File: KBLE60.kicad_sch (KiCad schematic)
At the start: 69 parts

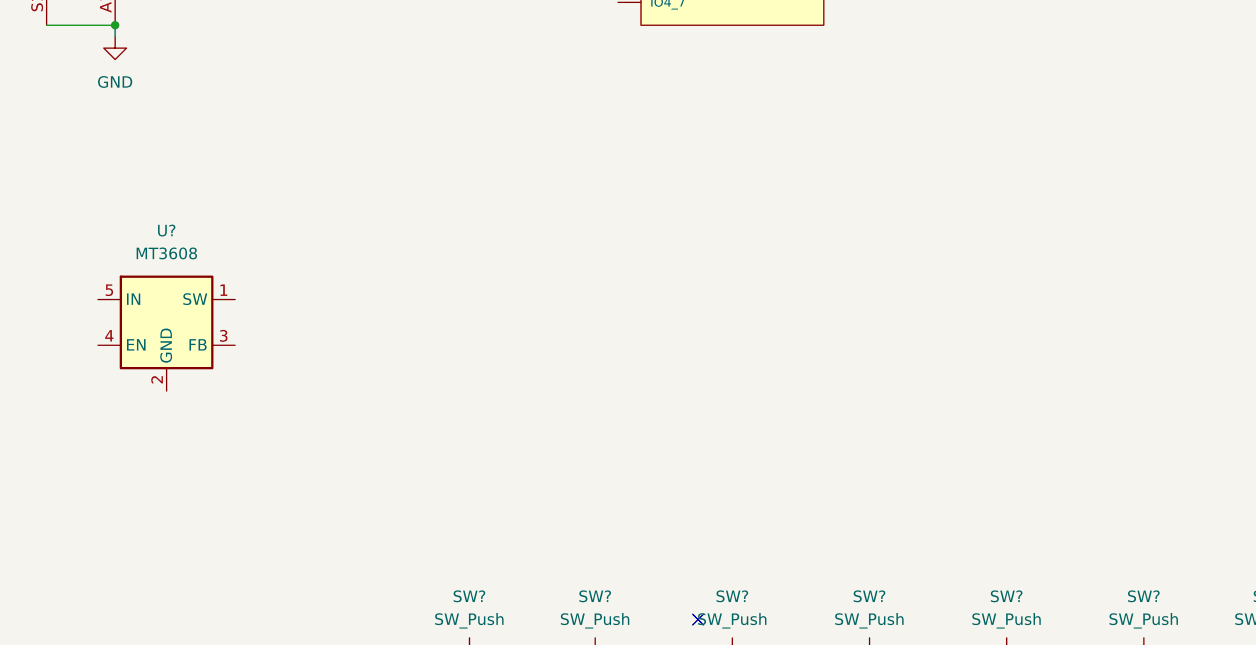
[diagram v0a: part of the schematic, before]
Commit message: battery charging ic
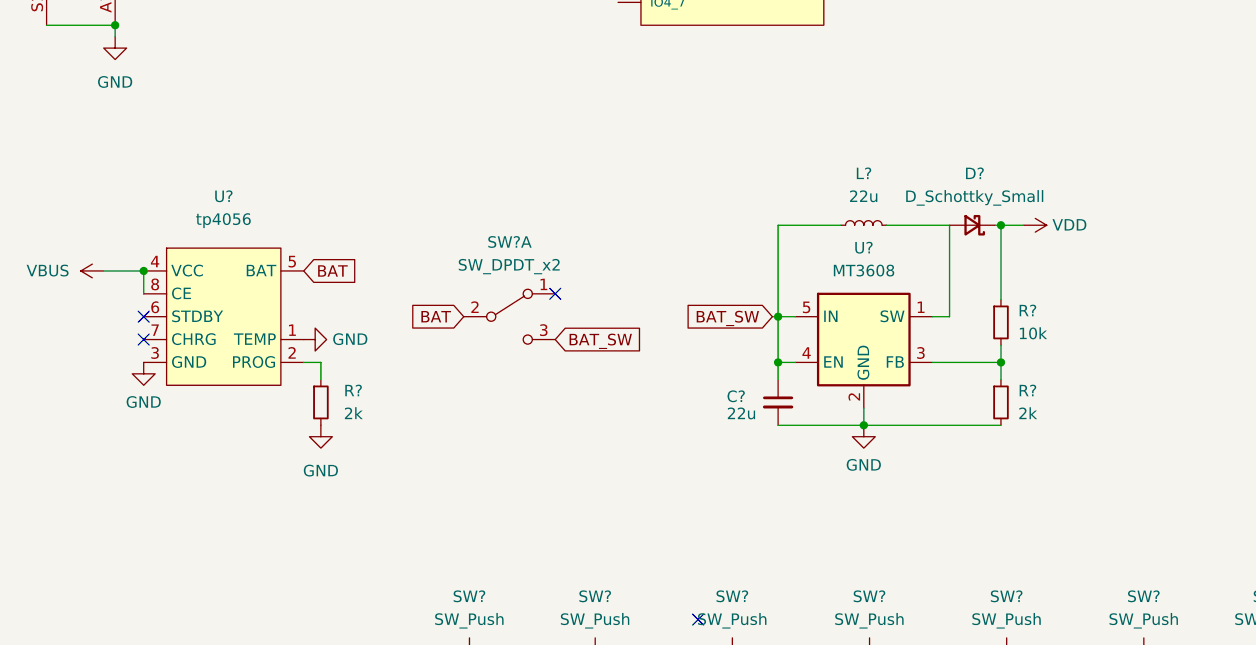
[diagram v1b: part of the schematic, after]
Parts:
- added C?: 22u, symbol Device:C_Small
- added D?: D_Schottky_Small, symbol Device:D_Schottky_Small
- added L?: 22u, symbol Device:L_Small
- added R?: 10k, symbol Device:R_Small
- added R? (x2): 2k, symbol Device:R_Small
- added SW?: SW_DPDT_x2, symbol Switch:SW_DPDT_x2
- added U?: tp4056, Package_SO:TSSOP-8_3x3mm_P0.65mm, symbol TP4056:tp4056
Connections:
- net GND: now also U?.2 (GND), C?.2, R?.2, R?.2, U?.1 (TEMP), U?.3 (GND)
- net VBUS: now also U?.4 (VCC), U?.8 (CE)
- net VDD: now also D?.1 (K), R?.1
- net at U?.1 (SW): now also D?.2 (A), L?.2
- net at U?.3 (FB): now also R?.1, R?.2
- net BAT_SW: now reaches U?.4 (EN)
- net BAT_SW: now also U?.5 (IN), C?.1, L?.1, SW?.3 (C)
- new net: R?.1, U?.2 (PROG)
- new net BAT: SW?.2 (B), U?.5 (BAT)
- no-connect marks 12 -> 15
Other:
- moved on the sheet: U?

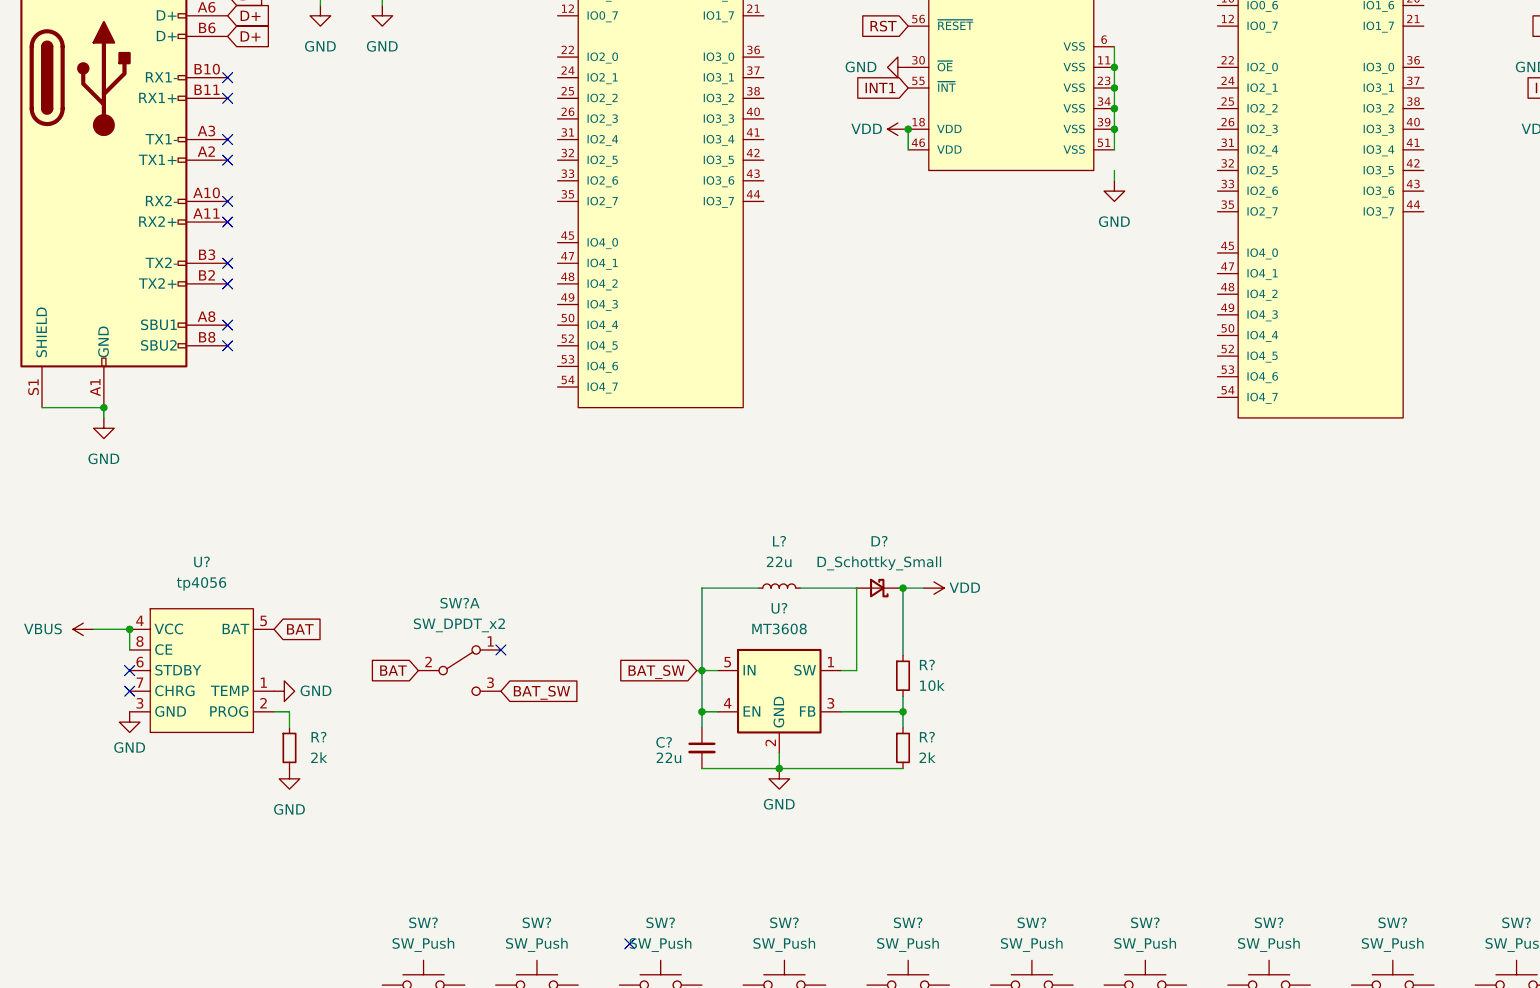
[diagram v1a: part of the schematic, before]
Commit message: Add protection ic
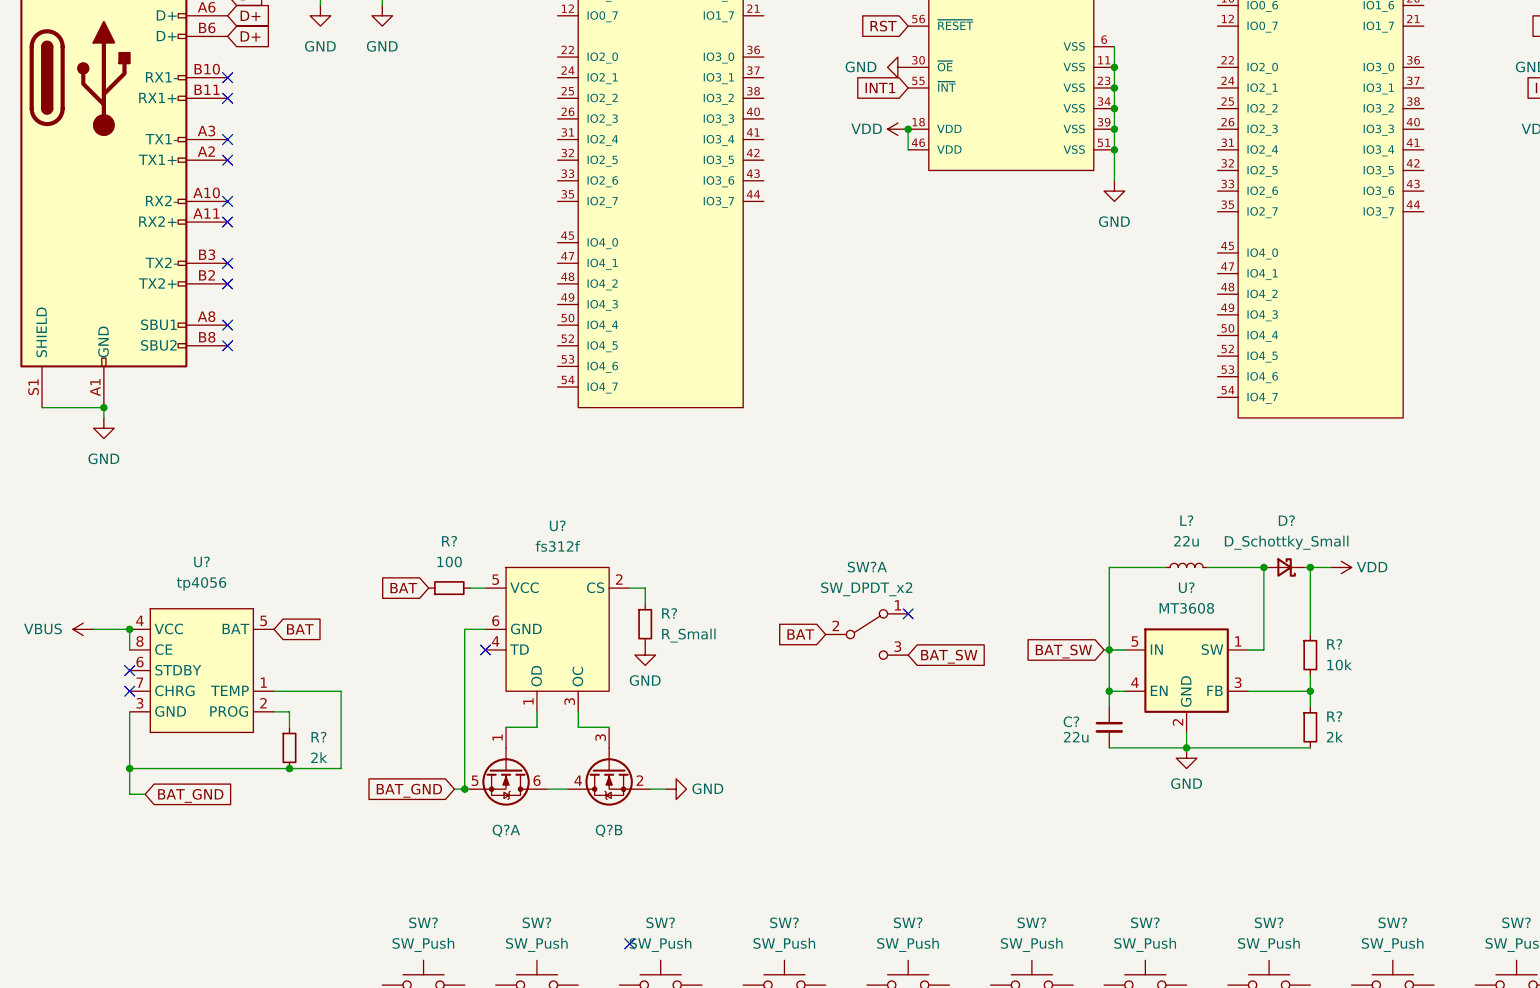
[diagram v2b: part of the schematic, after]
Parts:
- added Q? (x2): Q_Dual_NMOS_G1S2G2D2S1D1, symbol Device:Q_Dual_NMOS_G1S2G2D2S1D1
- added R?: 100, symbol Device:R_Small
- added R?: R_Small, symbol Device:R_Small
- added U?: fs312f, symbol FS312F:fs312f
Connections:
- net BAT: now also R?.1
- net GND: now also U?.11 (VSS), U?.23 (VSS), U?.34 (VSS), U?.39 (VSS), U?.51 (VSS), U?.6 (VSS), Q?.2 (S), R?.2; no longer R?.2, U?.1 (TEMP), U?.3 (GND)
- new net: Q?.3 (G), U?.3 (OC)
- new net: Q?.4 (D), Q?.6 (D)
- new net: R?.2, U?.5 (VCC)
- new net: Q?.1 (G), U?.1 (OD)
- new net: R?.1, U?.2 (CS)
- new net BAT_GND: Q?.5 (S), R?.2, U?.1 (TEMP), U?.3 (GND), U?.6 (GND)
- no-connect marks 15 -> 16
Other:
- moved on the sheet: C?, D?, L?, R?, SW?A, U?

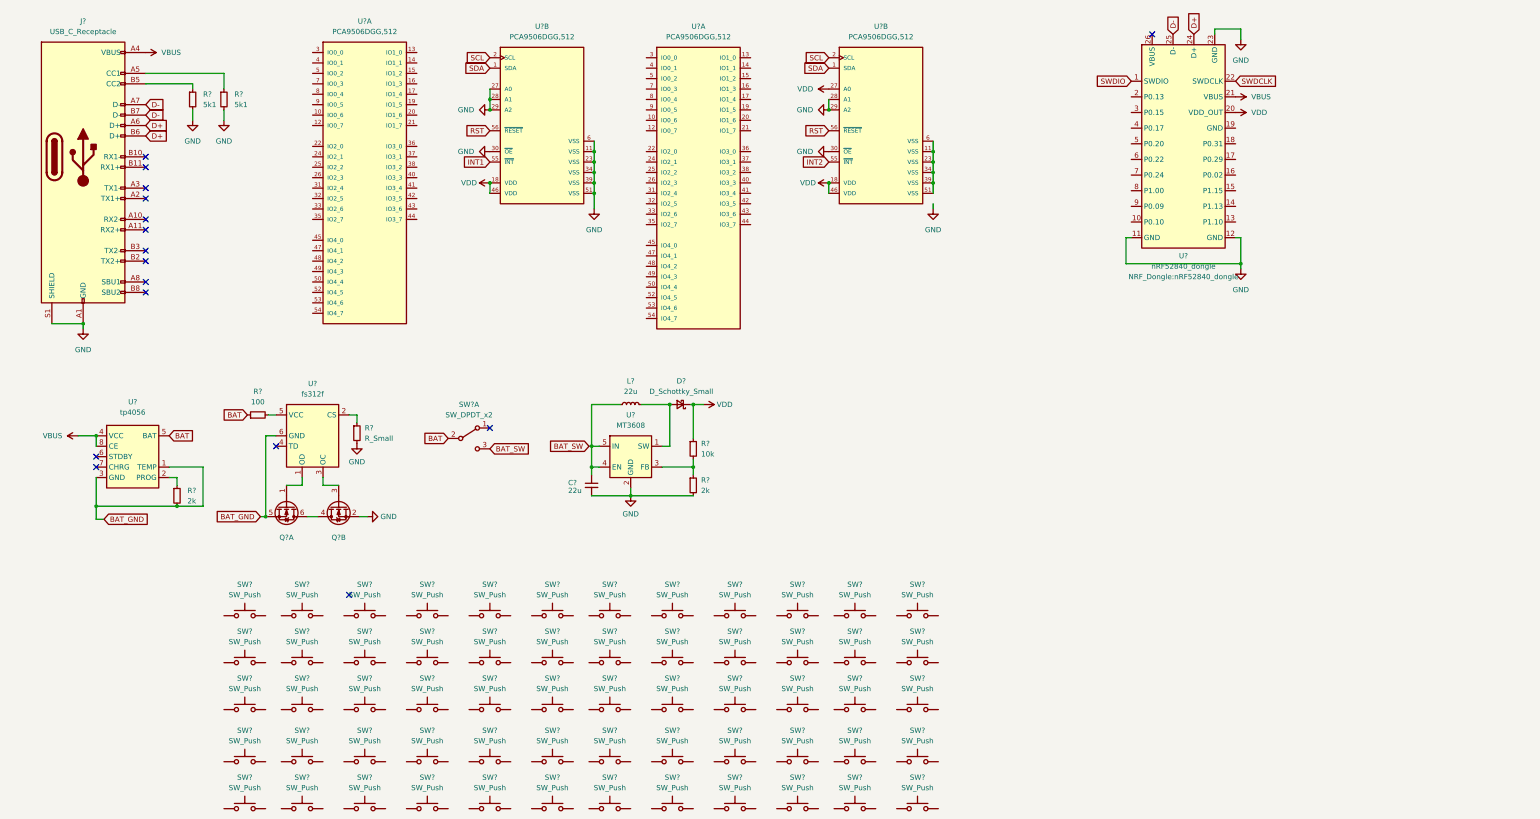
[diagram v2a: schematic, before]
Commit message: Key switchs and pull ups
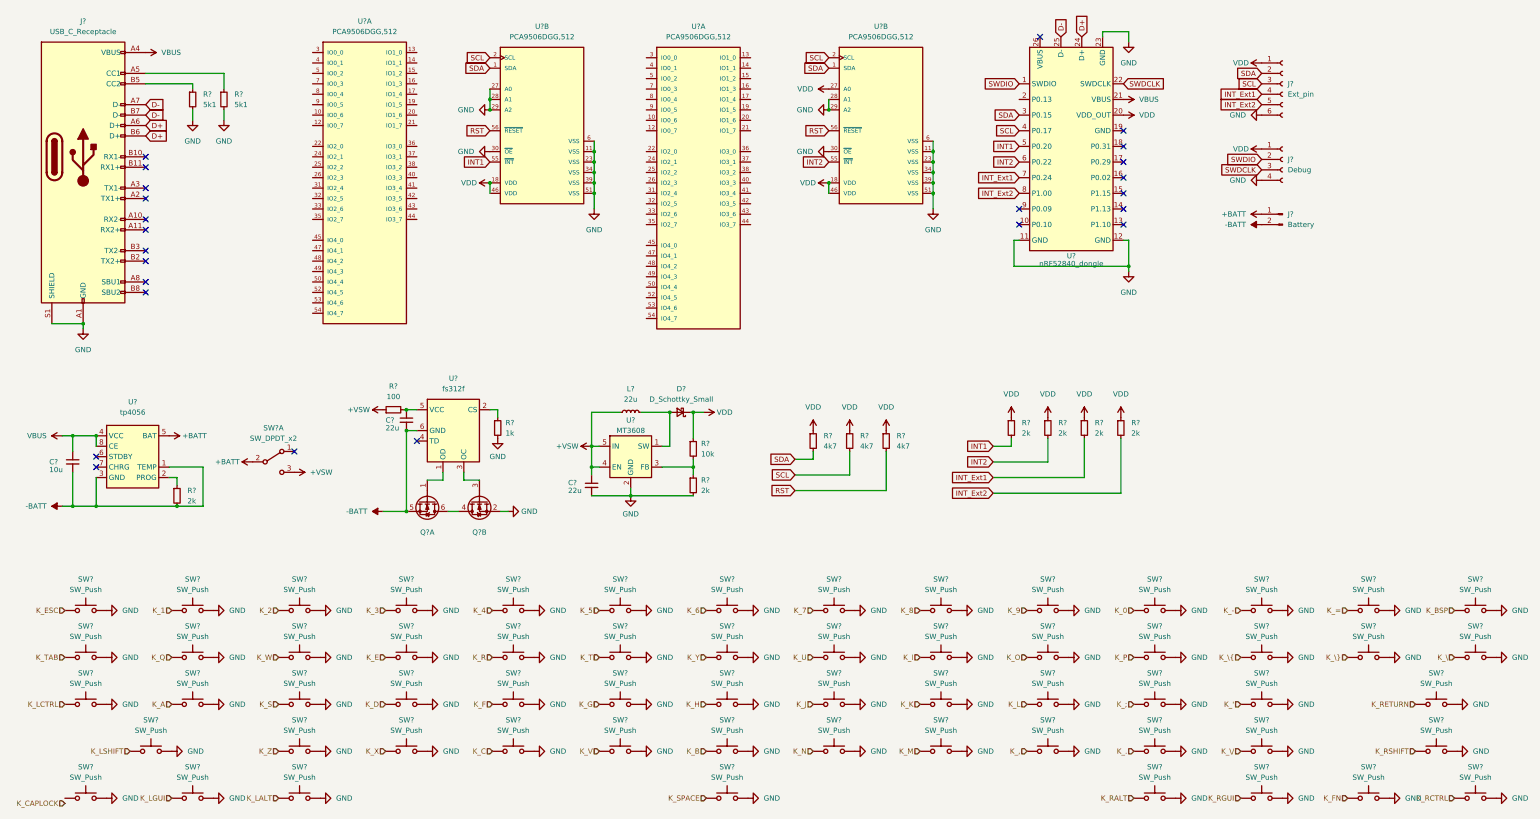
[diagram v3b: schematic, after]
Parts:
- removed R?: 100, symbol Device:R_Small
- removed SW? (x55): SW_Push, symbol Switch:SW_Push
- added C?: 10u, symbol Device:C_Small
- added C?: 22u, symbol Device:C_Small
- added J?: Ext_pin, symbol Connector:Conn_01x06_Female
- added J?: Battery, symbol Connector:Conn_01x02_Male
- added J?: Debug, symbol Connector:Conn_01x04_Female
- added R? (x3): 4k7, symbol Device:R_Small
- added R? (x4): 2k, symbol Device:R_Small
- added R?: 100, symbol Device:R_Small
- added SW? (x56): SW_Push, symbol Switch:SW_Push
- R?: value R_Small -> 1k
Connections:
- net GND: now also SW?.2, SW?.2, SW?.2, SW?.2, SW?.2, U?.11 (VSS), U?.23 (VSS), U?.34 (VSS), U?.39 (VSS), U?.51 (VSS), U?.6 (VSS), J?.4 (Pin_4), J?.6 (Pin_6), SW?.2, SW?.2, SW?.2, SW?.2, SW?.2, SW?.2, SW?.2, SW?.2, SW?.2, SW?.2, SW?.2, SW?.2, SW?.2, SW?.2, SW?.2, SW?.2, SW?.2, SW?.2, SW?.2, SW?.2, SW?.2, SW?.2, SW?.2, SW?.2, SW?.2, SW?.2, SW?.2, SW?.2, SW?.2, SW?.2, SW?.2, SW?.2, SW?.2, SW?.2, SW?.2, SW?.2, SW?.2, SW?.2, SW?.2, SW?.2, SW?.2, SW?.2, SW?.2, SW?.2, SW?.2, SW?.2, SW?.2, SW?.2, SW?.2, SW?.2, SW?.2, SW?.2, SW?.2, SW?.2, SW?.2, SW?.2
- net INT1: now also U?.5 (P0.20), R?.2
- net INT2: now also U?.6 (P0.22), R?.2
- net RST: now also R?.2
- net SCL: now also U?.4 (P0.17), J?.3 (Pin_3), R?.2
- net SDA: now also U?.3 (P0.15), J?.2 (Pin_2), R?.2
- net SWDCLK: now also J?.3 (Pin_3)
- net SWDIO: now also J?.2 (Pin_2)
- net VBUS: now also C?.1
- net VDD: now also J?.1 (Pin_1), J?.1 (Pin_1), R?.1, R?.1, R?.1, R?.1, R?.1, R?.1, R?.1
- net K_LSHIFT: now reaches SW?.1
- net K_TAB: now reaches SW?.1
- net at U?.5 (VCC): now also C?.1, R?.2
- net INT_Ext1: now reaches U?.7 (P0.24)
- net INT_Ext1: now also J?.4 (Pin_4), R?.2
- net INT_Ext2: now reaches U?.8 (P1.00)
- net INT_Ext2: now also J?.5 (Pin_5), R?.2
- net K_LCTRL: now reaches SW?.1
- net K_ESC: now reaches SW?.1
- net BAT renamed +BATT
- net +BATT: now also J?.1 (Pin_1)
- net BAT_GND renamed -BATT
- net -BATT: now also C?.2, C?.2, J?.2 (Pin_2)
- net BAT_SW renamed +VSW
- net +VSW: now also R?.1
- new net K_': SW?.1
- new net K_,: SW?.1
- new net K_-: SW?.1
- new net K_.: SW?.1
- new net K_0: SW?.1
- new net K_1: SW?.1
- new net K_2: SW?.1
- new net K_3: SW?.1
- new net K_4: SW?.1
- new net K_5: SW?.1
- new net K_6: SW?.1
- new net K_7: SW?.1
- new net K_8: SW?.1
- new net K_9: SW?.1
- new net K_;: SW?.1
- new net K_=: SW?.1
- new net K_A: SW?.1
- new net K_B: SW?.1
- new net K_BSP: SW?.1
- new net K_C: SW?.1
- new net K_D: SW?.1
- new net K_E: SW?.1
- new net K_F: SW?.1
- new net K_FN: SW?.1
- new net K_G: SW?.1
- new net K_H: SW?.1
- new net K_I: SW?.1
- new net K_J: SW?.1
- new net K_K: SW?.1
- new net K_L: SW?.1
- new net K_LALT: SW?.1
- new net K_LGUI: SW?.1
- new net K_M: SW?.1
- new net K_N: SW?.1
- new net K_O: SW?.1
- new net K_P: SW?.1
- new net K_Q: SW?.1
- new net K_R: SW?.1
- new net K_RALT: SW?.1
- new net K_RCTRL: SW?.1
- new net K_RETURN: SW?.1
- new net K_RGUI: SW?.1
- new net K_RSHIFT: SW?.1
- new net K_S: SW?.1
- new net K_SPACE: SW?.1
- new net K_T: SW?.1
- new net K_U: SW?.1
- new net K_V: SW?.1
- new net K_W: SW?.1
- new net K_X: SW?.1
- new net K_Y: SW?.1
- new net K_Z: SW?.1
- new net K_\: SW?.1
- new net K_\{: SW?.1
- new net K_\/: SW?.1
- new net K_\}: SW?.1
- no-connect marks 16 -> 24
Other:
- moved on the sheet: D?, L?, Q?A, Q?B, R?, SW?, SW?A, U?

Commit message: Sch and footprints
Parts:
- C1, C2, C3: renamed from C?; footprint (none) -> Capacitor_SMD:C_0201_0603Metric_Pad0.64x0.40mm_HandSolder
- D1: renamed from D?; footprint (none) -> Diode_SMD:D_0201_0603Metric_Pad0.64x0.40mm_HandSolder
- J1: renamed from J?; footprint (none) -> Connector_USB:USB_C_Receptacle_HRO_TYPE-C-31-M-12
- J2: renamed from J?; footprint (none) -> Connector_PinHeader_1.00mm:PinHeader_1x06_P1.00mm_Vertical
- J3: renamed from J?; footprint (none) -> Connector_PinHeader_2.54mm:PinHeader_1x04_P2.54mm_Vertical
- J4: renamed from J?; footprint (none) -> Connector_Molex:Molex_KK-254_AE-6410-02A_1x02_P2.54mm_Vertical
- L1: renamed from L?; footprint (none) -> Inductor_SMD:L_0201_0603Metric_Pad0.64x0.40mm_HandSolder
- Q1: renamed from Q?; footprint (none) -> Package_TO_SOT_SMD:SOT-363_SC-70-6
- R1, R10, R11, R12, R13, R14, R2, R3, R4, R5, R6, R7, R8, R9: renamed from R?; footprint (none) -> Resistor_SMD:R_0201_0603Metric_Pad0.64x0.40mm_HandSolder
- SW1, SW11, SW12, SW13, SW14, SW16, SW17, SW18, SW19, SW20, SW21, SW22, SW23, SW24, SW25, SW26, SW27, SW28, SW29, SW30, SW31, SW33, SW34, SW35, SW36, SW37, SW38, SW39, SW40, SW41, SW42, SW43, SW44, SW45, SW46, SW47, SW48, SW50, SW51, SW52, SW53, SW55, SW56, SW6, SW7, SW8: renamed from SW?; footprint (none) -> Button_Switch_Keyboard:SW_Cherry_MX_1.00u_PCB
- SW10: renamed from SW?; footprint (none) -> Button_Switch_THT:SW_CuK_JS202011AQN_DPDT_Angled
- SW15, SW4, SW49, SW54, SW57, SW62, SW9: renamed from SW?; footprint (none) -> Button_Switch_Keyboard:SW_Cherry_MX_1.25u_PCB
- SW2, SW61: renamed from SW?; footprint (none) -> Button_Switch_Keyboard:SW_Cherry_MX_1.50u_PCB
- SW3: renamed from SW?; footprint (none) -> Button_Switch_Keyboard:SW_Cherry_MX_1.75u_PCB
- SW32: renamed from SW?; footprint (none) -> Button_Switch_Keyboard:SW_Cherry_MX_6.25u_PCB
- SW5, SW58, SW60: renamed from SW?; footprint (none) -> Button_Switch_Keyboard:SW_Cherry_MX_2.25u_PCB
- SW59: renamed from SW?; footprint (none) -> Button_Switch_Keyboard:SW_Cherry_MX_2.75u_PCB
- U2, U5: renamed from U?; footprint NXP_Semiconductors-PCA9506DGG,512-* -> Package_SO:TSSOP-56_6.1x14mm_P0.5mm
- U3: renamed from U?; footprint (none) -> Package_TO_SOT_SMD:SOT-23-6_Handsoldering
- gave numbers to parts that had none: 3
